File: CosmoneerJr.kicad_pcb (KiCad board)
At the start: 4 copper layers, 70 x 50 mm, 82 parts, among them J1 Header, J13 Header, J17 Header, J18 Header, J5 Header, J9 Header, P1 .1" Header, P2 Header, P3 SM04B-SRSS-TB, P4 Header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

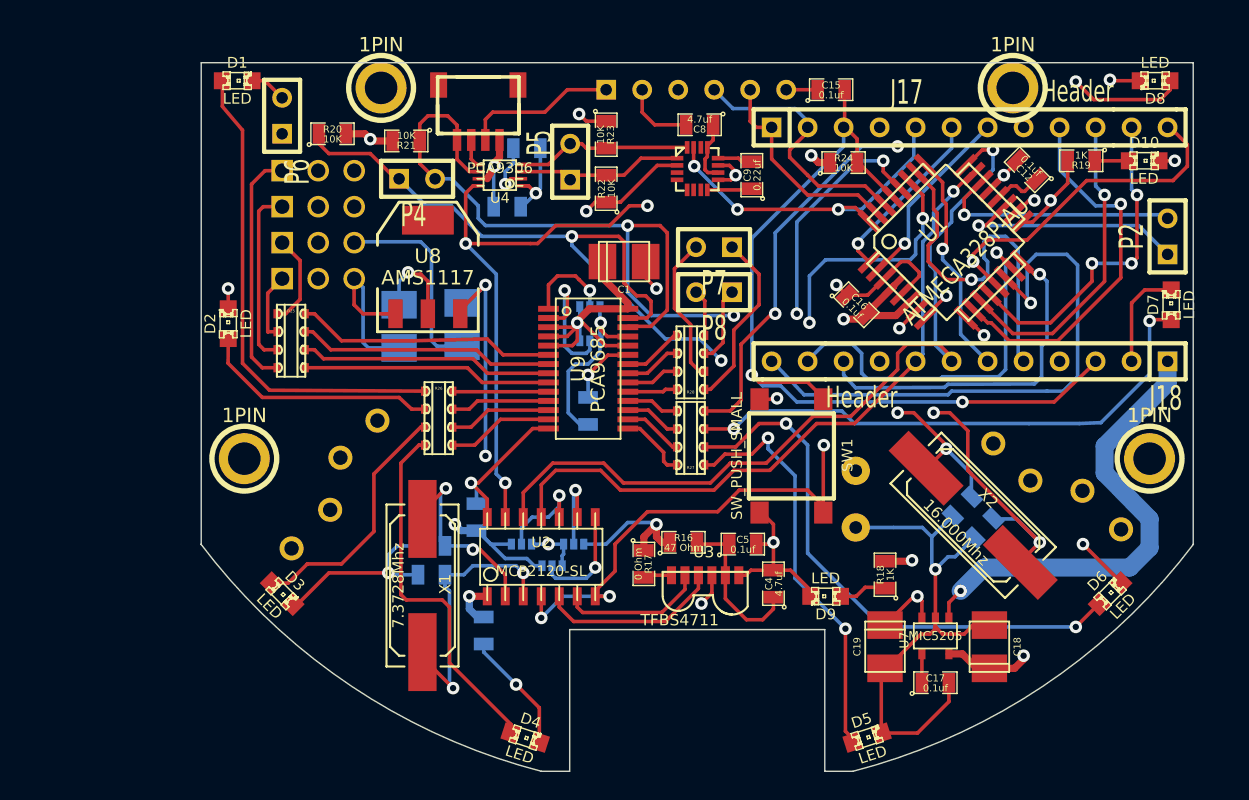
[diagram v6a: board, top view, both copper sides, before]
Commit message: Rev Zero Prototype
Silkscreen cleanup, minor part movements
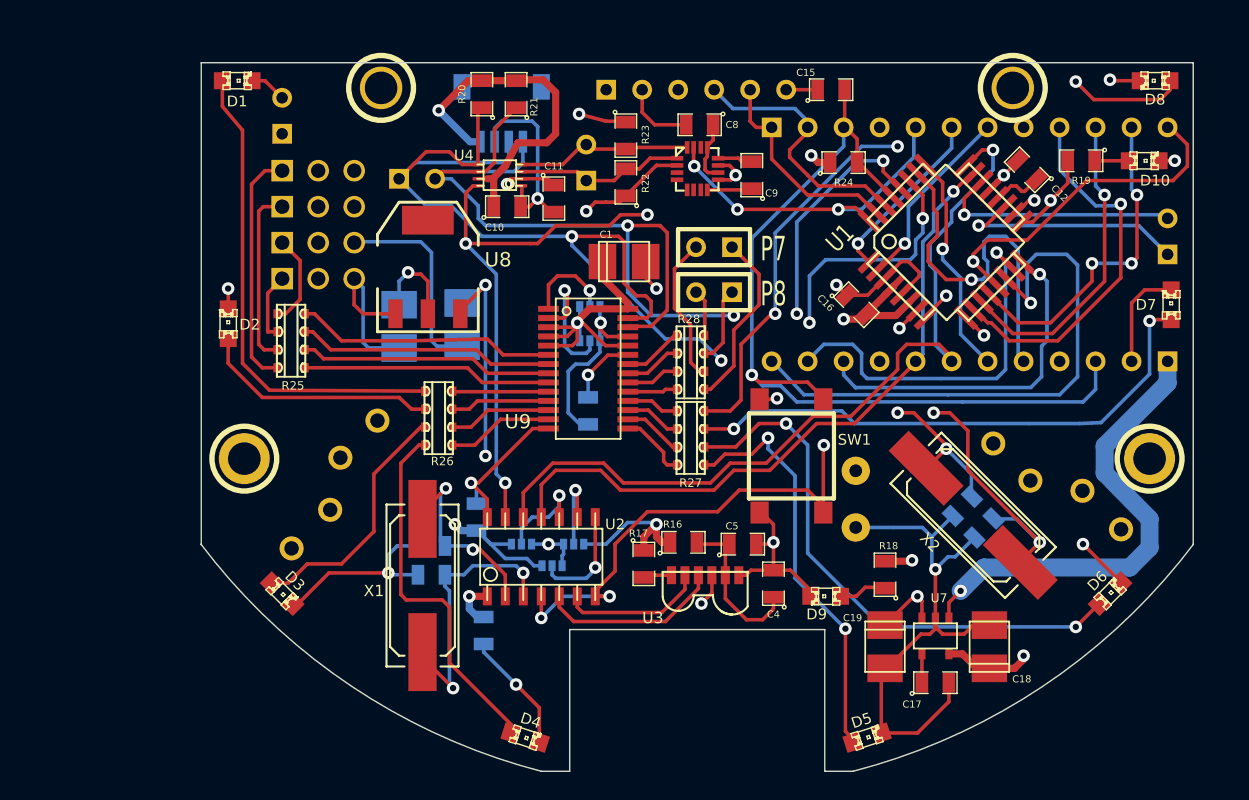
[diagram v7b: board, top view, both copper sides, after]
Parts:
- C10, C11: moved to F.Cu
- J17, J18, P2, P3, P4, P5, P6: moved to B.Cu
- moved R20 10.9 mm to (209.8, 117.2), turned to 90 degrees
- moved R21 8.42 mm to (212.2, 117.2), turned to 90 degrees
- moved C11 4.03 mm to (214.9, 124.6), turned to 270 degrees
- moved P3 1.66 mm to (211.2, 117.6), turned to 0 degrees
- moved R22 1.46 mm to (220.0, 123.4)
- moved R23 1.39 mm to (220.0, 120.1)
- moved P5 1.14 mm to (217.2, 122.0)
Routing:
- net +5V: track 76.6 -> 91.9 mm, vias 11 -> 10
- net /I2C_SDA_5V: track 74.4 -> 85.4 mm
- net /I2C_SCL_5V: track 74.0 -> 79.6 mm
- net +3.3V: track 46.0 -> 49.4 mm
- net GND: track 209.2 -> 206.3 mm
- net /RESET: track 104.5 -> 105.7 mm, vias 5 -> 4
